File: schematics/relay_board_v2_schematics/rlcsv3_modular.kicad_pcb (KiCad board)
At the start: 2 copper layers, 45 x 75 mm, 46 parts, among them J1 Programming Header, P1 ACT_PWR, P2 ACT_PWR, Q1 MMBF170, Q2 MMBF170, U1 SPST_POWER_RELAY, U2 PIC16F1826-ISO, U3 dpdt_relay, U4 INA180A1, U5 CONN_01x05, U6 INA180A1, U7 CONN_01x05

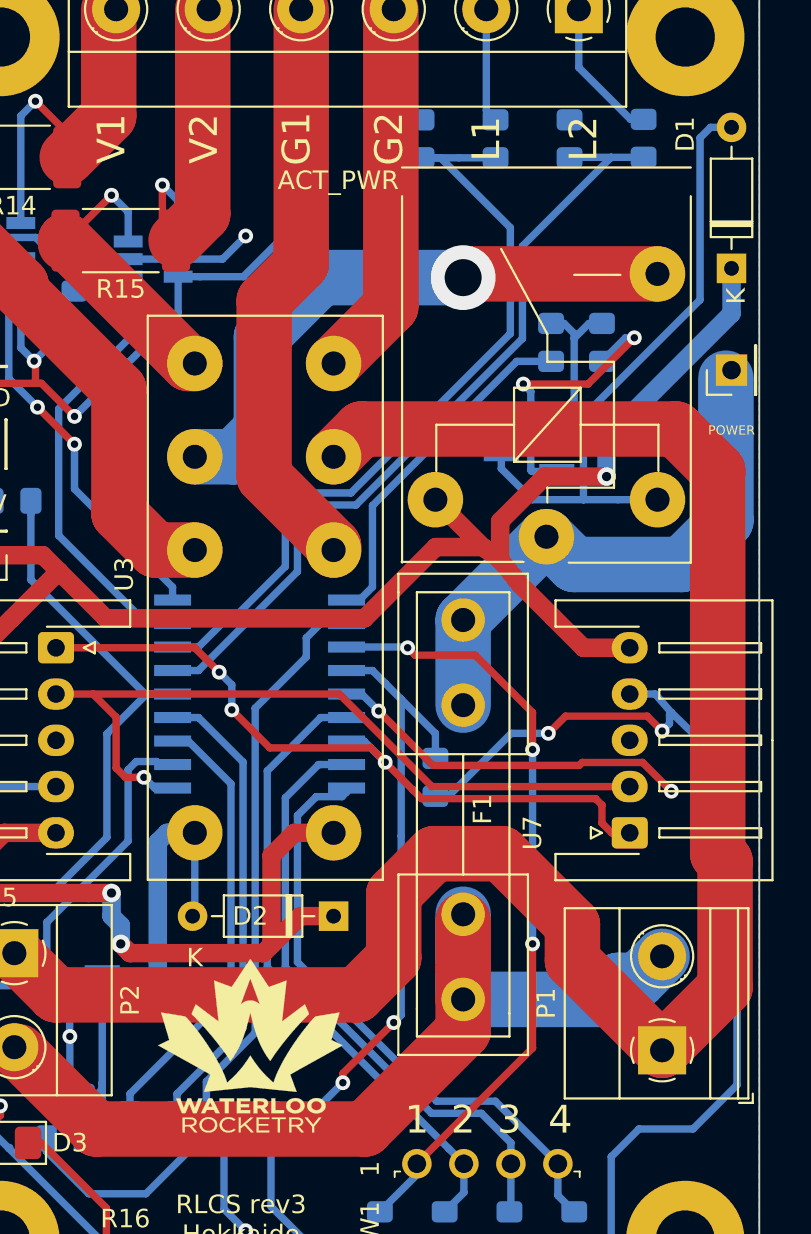
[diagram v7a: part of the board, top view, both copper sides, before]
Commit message: Add changes to address Zach's comments
Signed-off-by: AIDAN HA <qbha@edu.uwaterloo.ca>
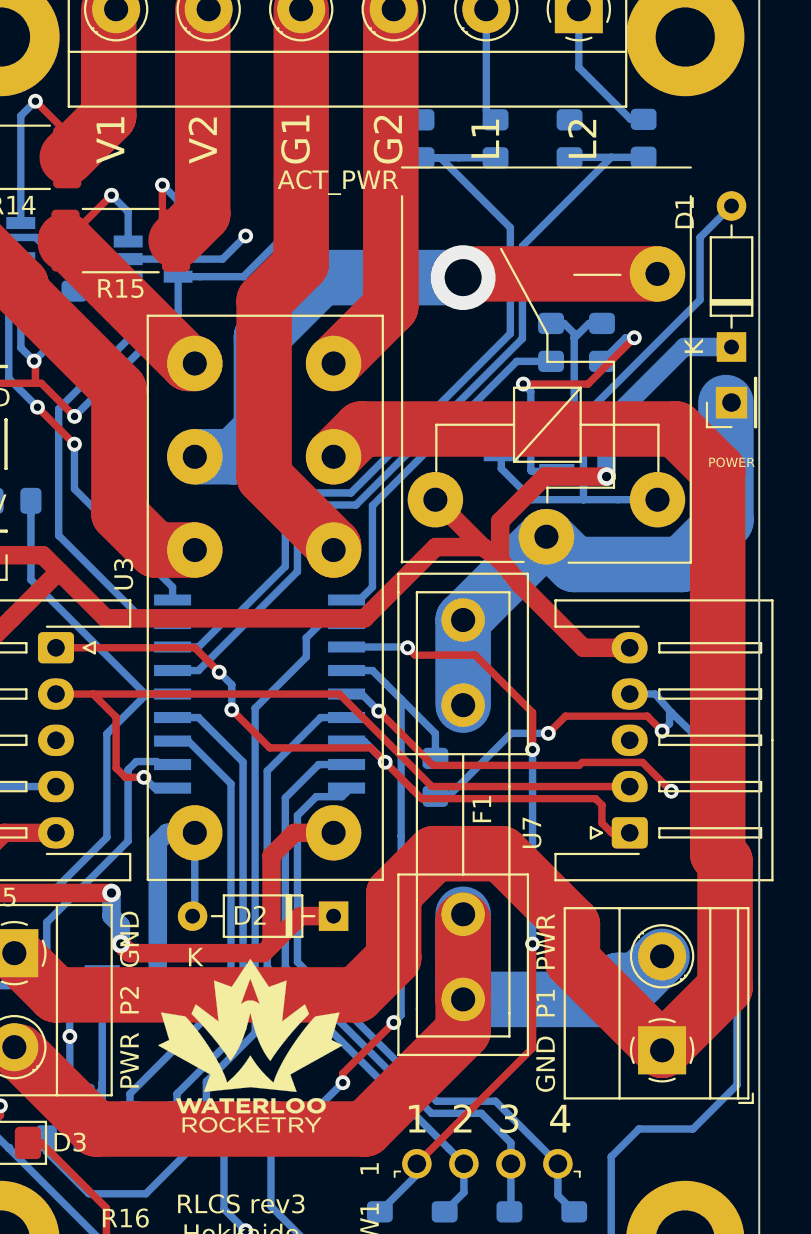
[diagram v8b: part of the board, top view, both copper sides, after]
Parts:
- GND  P1  PWR: renamed from P1
- PWR  P2  GND: renamed from P2
- moved D1 4.25 mm to (173.5, 90.8)
- moved POWER 1.75 mm to (173.5, 93.8)
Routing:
- net Net-(D1-Pad2): track 34.0 -> 29.1 mm
- net +12V: track 120.5 -> 117.7 mm
- net Net-(F1-Pad2): track 31.2 -> 29.8 mm
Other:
- board text added: "12V 5V GND SCL SDA"
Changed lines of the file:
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@@
   (general
     (thickness 1.6)
-    (drawings 16)
-    (tracks 472)
+    (drawings 18)
+    (tracks 471)
     (zones 0)
     (modules 46)
@@
     (descr "Terminal Block Phoenix MKDS-1,5-2-5.08, 2 pins, pitch 5.08mm, size 10.2x9.8mm^2, drill diamater 1.3mm, pad diameter 2.6mm, see http://www.farnell.com/datasheets/100425.pdf, script-generated using https://github.com/pointhi/kicad-footprint-generator/scripts/TerminalBlock_Phoenix")
     (tags "THT Terminal Block Phoenix MKDS-1,5-2-5.08 pitch 5.08mm size 10.2x9.8mm^2 drill 1.3mm pad 2.6mm")
-    (fp_text reference P2 (at 2.54 -6.26 90) (layer F.SilkS)
+    (fp_text reference "PWR  P2  GND" (at 2.54 -6.26 90) (layer F.SilkS)
       (effects (font (size 1 1) (thickness 0.15)))
     )
@@
   )
   (module Socket_Strips:Socket_Strip_Straight_1x01_Pitch2.54mm (layer F.Cu)
-    (at 173.5 92 90)
+    (at 173.5 93.75 90)
     (descr "Through hole straight socket strip, 1x01, 2.54mm pitch, single row")
     (tags "Through hole socket strip THT 1x01 2.54mm single row")
@@
   )
   (module Diode_THT:D_DO-35_SOD27_P7.62mm_Horizontal (layer F.Cu)
-    (at 173.5 86.5 90)
+    (at 173.5 90.75 90)
     (descr "Diode, DO-35_SOD27 series, Axial, Horizontal, pin pitch=7.62mm, , length*diameter=4*2mm^2, , http://www.diodes.com/_files/packages/DO-35.pdf")
     (tags "Diode DO-35_SOD27 series Axial Horizontal pin pitch 7.62mm  length 4mm diameter 2mm")
@@
       (effects (font (size 1 1) (thickness 0.15)))
     )
-    (fp_text user K (at -1.5 0.25 90) (layer F.SilkS)
+    (fp_text user K (at 0 -2 90) (layer F.SilkS)
       (effects (font (size 1 1) (thickness 0.15)))
     )
@@
     (descr "Terminal Block Phoenix MKDS-1,5-2-5.08, 2 pins, pitch 5.08mm, size 10.2x9.8mm^2, drill diamater 1.3mm, pad diameter 2.6mm, see http://www.farnell.com/datasheets/100425.pdf, script-generated using https://github.com/pointhi/kicad-footprint-generator/scripts/TerminalBlock_Phoenix")
     (tags "THT Terminal Block Phoenix MKDS-1,5-2-5.08 pitch 5.08mm size 10.2x9.8mm^2 drill 1.3mm pad 2.6mm")
-    (fp_text reference P1 (at 2.54 -6.26 90) (layer F.SilkS)
+    (fp_text reference "GND  P1  PWR" (at 2.54 -6.26 90) (layer F.SilkS)
       (effects (font (size 1 1) (thickness 0.15)))
     )
@@
     )
   )
+  (gr_text "12V 5V GND SCL SDA" (at 165.25 112 270) (layer B.SilkS)
+    (effects (font (size 0.8 0.8) (thickness 0.15)))
+  )
+  (gr_text "12V 5V GND SCL SDA" (at 134.75 111.75 90) (layer B.SilkS)
+    (effects (font (size 0.8 0.8) (thickness 0.15)))
+  )
   (gr_text "~MCLR 5V" (at 154 133.25 90) (layer B.SilkS)
     (effects (font (size 1 1) (thickness 0.15)) (justify mirror))
@@
   (segment (start 133.75 120.25) (end 138.75 120.25) (width 1) (layer F.Cu) (net 1))
   (segment (start 133.35 119.85) (end 133.75 120.25) (width 1) (layer F.Cu) (net 1))
-  (segment (start 166.75 95.692798) (end 166.75 97.75) (width 1) (layer B.Cu) (net 1))
-  (segment (start 173.5 88.942798) (end 166.75 95.692798) (width 1) (layer B.Cu) (net 1))
-  (segment (start 173.5 86.5) (end 173.5 88.942798) (width 1) (layer B.Cu) (net 1))
   (segment (start 140 121.5) (end 140.5 122) (width 1) (layer B.Cu) (net 1))
   (segment (start 140 120.25) (end 140 121.5) (width 1) (layer B.Cu) (net 1))
   (segment (start 138.75 120.25) (end 140 120.25) (width 1) (layer F.Cu) (net 1))
+  (segment (start 166.75 97.75) (end 166.75 94.95) (width 1) (layer B.Cu) (net 1))
+  (segment (start 170.95 90.75) (end 173.5 90.75) (width 1) (layer B.Cu) (net 1))
+  (segment (start 166.75 94.95) (end 170.95 90.75) (width 1) (layer B.Cu) (net 1))
   (segment (start 164.06 94.77) (end 165 93.83) (width 0.4) (layer B.Cu) (net 2))
   (segment (start 164.06 95.57) (end 164.06 94.77) (width 0.4) (layer B.Cu) (net 2))
@@
   (segment (start 171.800001 88.199999) (end 165.5 94.5) (width 0.4) (layer B.Cu) (net 10))
   (segment (start 165.5 94.5) (end 165.5 99) (width 0.4) (layer B.Cu) (net 10))
-  (segment (start 171.800001 79.448629) (end 171.800001 88.199999) (width 0.4) (layer B.Cu) (net 10))
-  (segment (start 172.36863 78.88) (end 171.800001 79.448629) (width 0.4) (layer B.Cu) (net 10))
-  (segment (start 173.5 78.88) (end 172.36863 78.88) (width 0.4) (layer B.Cu) (net 10))
+  (segment (start 171.800001 84.829999) (end 173.5 83.13) (width 0.4) (layer B.Cu) (net 10))
+  (segment (start 171.800001 88.199999) (end 171.800001 84.829999) (width 0.4) (layer B.Cu) (net 10))
   (segment (start 144.5 121.38) (end 144.38 121.5) (width 0.4) (layer B.Cu) (net 11))
   (segment (start 144.5 117) (end 144.5 121.38) (width 0.4) (layer B.Cu) (net 11))
@@
   (segment (start 163.5 101) (end 164.999999 102.499999) (width 3) (layer B.Cu) (net 12))
   (segment (start 159 105.5) (end 159 110.1) (width 3) (layer B.Cu) (net 12))
-  (segment (start 173.19599 100.119932) (end 173.19599 92.434458) (width 3) (layer B.Cu) (net 12))
   (segment (start 170.815923 102.499999) (end 173.19599 100.119932) (width 3) (layer B.Cu) (net 12))
   (segment (start 164.999999 102.499999) (end 170.815923 102.499999) (width 3) (layer B.Cu) (net 12))
+  (segment (start 173.19599 100.119932) (end 173.19599 93.75) (width 3) (layer B.Cu) (net 12))
   (segment (start 154.808011 108.938011) (end 154.1 108.23) (width 0.4) (layer B.Cu) (net 13))
   (segment (start 154.1 108.23) (end 152.7 108.23) (width 0.4) (layer B.Cu) (net 13))
